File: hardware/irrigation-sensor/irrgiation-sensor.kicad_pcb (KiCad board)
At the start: 2 copper layers, 176 x 40 mm, 35 parts, among them J1 CONUFL001-SMD-T, J2 SHF-105-01-L-D-TH, Q1 PMV250EPEA, Q2 TSM260P02, U1 24LC32, U2 RFM95W, U3 TLV61225, U4 STM32L412KB

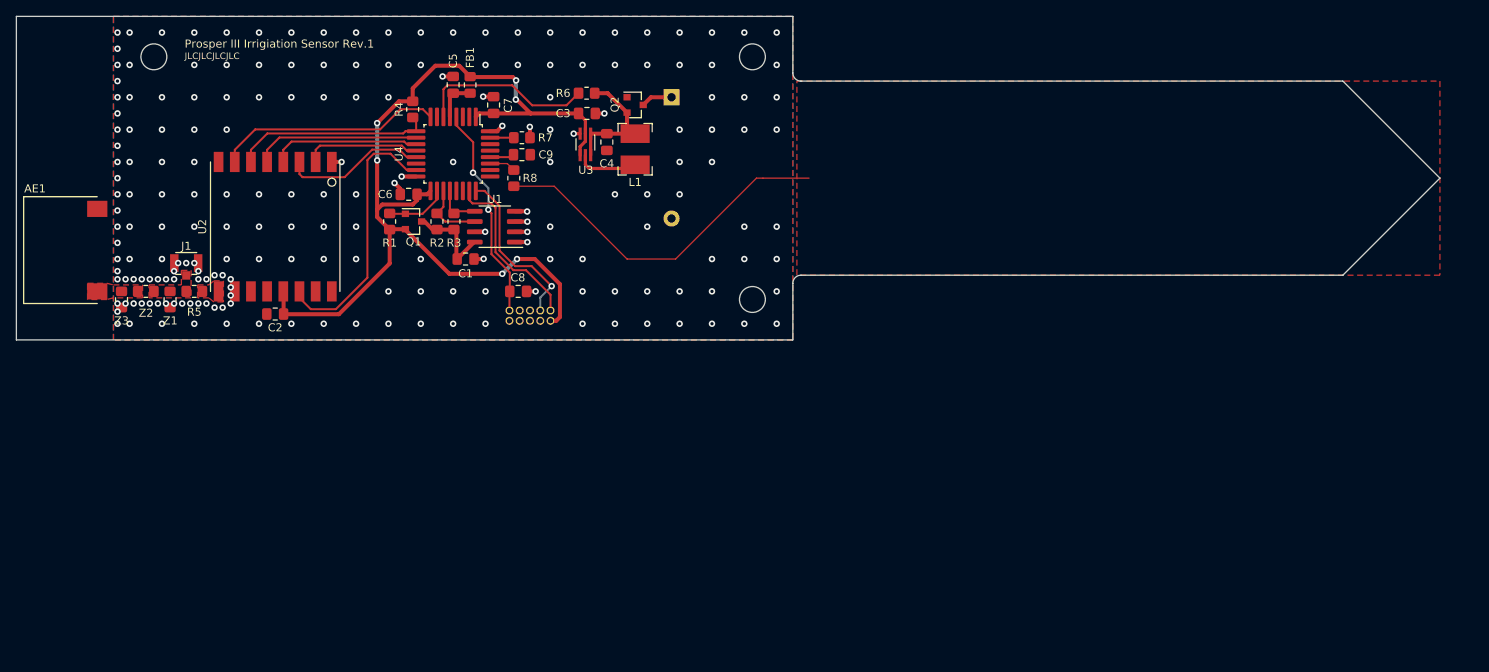
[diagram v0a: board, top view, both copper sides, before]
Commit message: PCB revision 2, add data packet handling to climate-sensor
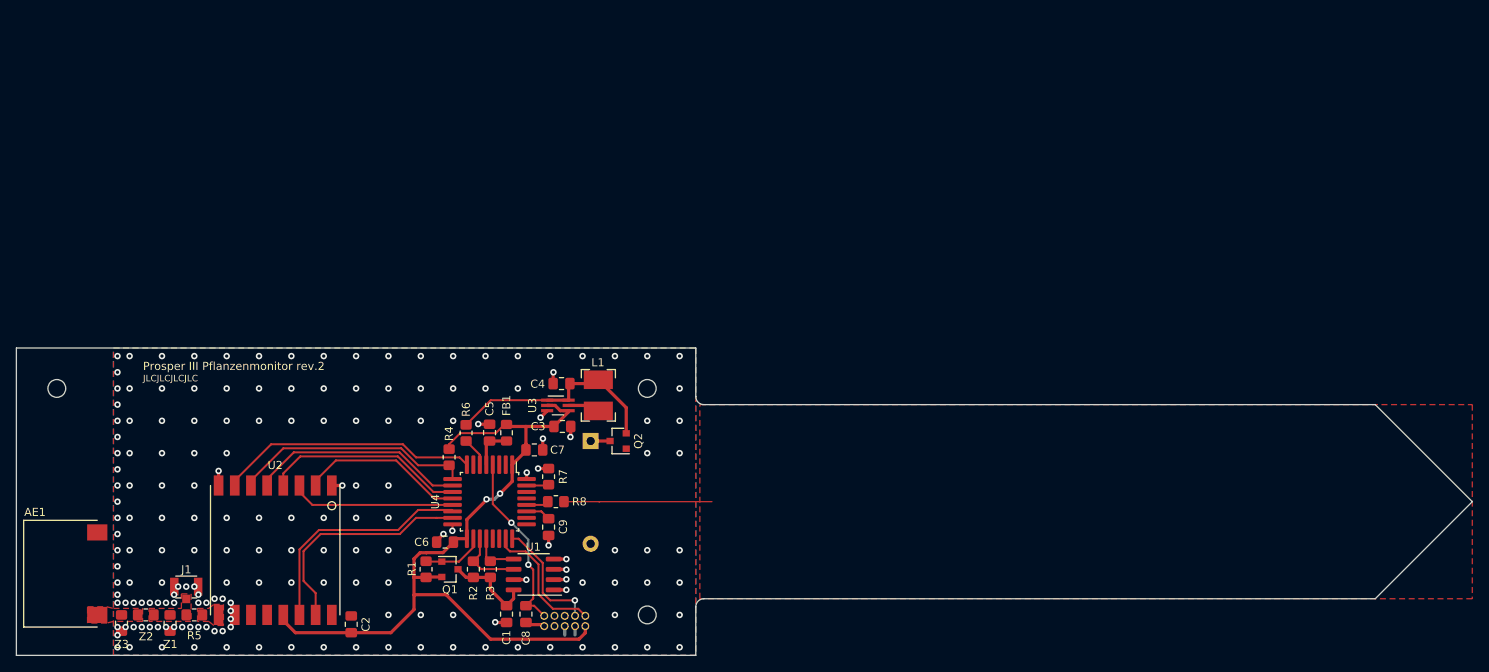
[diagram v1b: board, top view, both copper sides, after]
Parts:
- added G***: LOGO, my-footprints-library:ProsperIIIKlimaMonitorLogo, B.Cu at (65.0, 100.0)
- BT1: footprint my-footprints-library:BatteryHolder_Keystone_2462_2xAA_NoSilkscreen -> my-footprints-library:BatteryHolder_Keystone_2468_2xAAA_NoSilkscreen
- H1, H2, H3: footprint MountingHole:MountingHole_3.2mm_M3 -> MountingHole:MountingHole_2.2mm_M2
- moved C9 46.2 mm to (125.8, 103.1), turned to 270 degrees
- moved R6 44.6 mm to (115.6, 91.5), turned to 270 degrees
- moved C1 44.2 mm to (120.6, 113.9), turned to 270 degrees
- moved BT1 43.7 mm to (131.0, 92.5)
- moved U1 43.3 mm to (124.0, 109.0)
- moved C5 43.2 mm to (118.5, 91.5)
- moved C6 43.2 mm to (113.0, 105.0)
- moved Q1 43.2 mm to (113.6, 108.4)
- moved R1 43.2 mm to (110.7, 108.4)
- moved R2 43.2 mm to (116.5, 108.4)
- moved R3 43.2 mm to (118.6, 108.4)
- moved R4 43.2 mm to (113.5, 94.5)
- moved U4 43.2 mm to (118.5, 100.0)
- moved FB1 43.2 mm to (120.6, 91.5)
- moved H2 43.0 mm to (138.0, 86.0)
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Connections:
- C9 pad 1: TSC_IO2 -> TSC_IO1
- R8 pad 1: TSC_IO1 -> TSC_IO2
- U2 pad 14: RFM95_IRQ -> RFM95_DIO0
- U2 pad 15: Net-(U2-Pad15) -> RFM95_DIO1
- U4 pad 14: Net-(U4-Pad14) -> RFM95_DIO0
- U4 pad 15: RFM95_IRQ -> RFM95_DIO1
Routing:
- net RFM95_IRQ: track 33.1 -> 0.00 mm
- net RFM95_DIO0: track 0.00 -> 29.2 mm
- net RFM95_DIO1: track 0.00 -> 28.6 mm
- net SENSOR_PLANE: track 44.4 -> 18.4 mm
- net +3V3: track 120.7 -> 98.8 mm, vias 6 -> 2
- net Net-(R6-Pad2): track 22.0 -> 3.63 mm
- net VIN_SENSE: track 16.1 -> 27.8 mm
- net GND: track 22.2 -> 29.5 mm, vias 202 -> 183
- net SCK: track 18.5 -> 25.1 mm
- net RFM95_NSS: track 20.6 -> 26.8 mm
- net MISO: track 14.4 -> 20.5 mm
- net SWCLK: track 21.1 -> 15.0 mm
- net RFM95_NRST: track 24.8 -> 29.5 mm
- net SWDIO: track 21.2 -> 16.6 mm
- net NRST: track 26.7 -> 22.7 mm
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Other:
- board size 176 x 40 mm -> 180 x 38 mm
- board text added: "Prosper III Pflanzenmonitor rev.2"
- board text removed: "Prosper III Irrigiation Sensor Rev.1"

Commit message: Implement user management and authorization
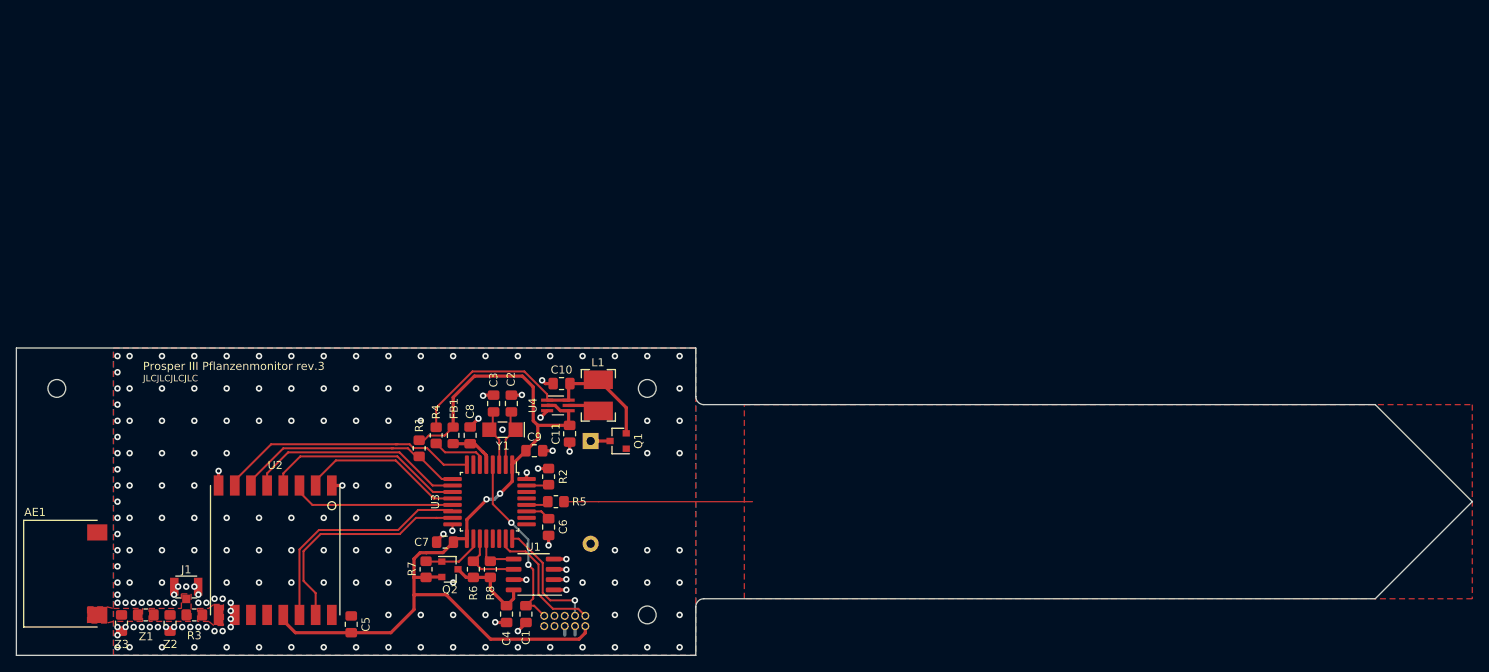
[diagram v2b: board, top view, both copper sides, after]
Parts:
- removed the G*** at (65.0, 100.0)
- added C2: 100nF, Capacitor_SMD:C_0805_2012Metric_Pad1.18x1.45mm_HandSolder, F.Cu at (121.2, 87.9)
- added C3: 100nF, Capacitor_SMD:C_0805_2012Metric_Pad1.18x1.45mm_HandSolder, F.Cu at (119.0, 87.9)
- added G***: LOGO, my-footprints-library:ProsperIIIPflanzenMonitorLogo, B.Cu at (66.0, 103.5)
- added Y1: 32768Hz, Crystal:Crystal_SMD_EuroQuartz_EQ161-2Pin_3.2x1.5mm_HandSoldering, F.Cu at (120.1, 91.1)
- moved FB1 6.61 mm to (114.0, 91.8)
- moved R1 3.86 mm to (109.8, 93.4)
- moved R4 3.71 mm to (111.9, 91.8)
- moved C8 2.42 mm to (116.1, 91.8)
- moved C11 1.27 mm to (128.4, 91.6), turned to 270 degrees
- moved C9 0.10 mm to (124.0, 93.7)
- renumbered C8 to C1, C4 to C10, C3 to C11, C1 to C4, C2 to C5, C9 to C6, C6 to C7, C5 to C8, C7 to C9, Q2 to Q1, Q1 to Q2, R4 to R1, R7 to R2, R5 to R3, R6 to R4, R8 to R5, R2 to R6, R1 to R7, R3 to R8, U4 to U3, U3 to U4, Z2 to Z1, Z1 to Z2
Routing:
- net +3V3: track 98.8 -> 112.9 mm
- net VIN_SENSE: track 27.8 -> 36.4 mm
- net Net-(C2-Pad1): track 0.00 -> 7.27 mm
- net Net-(C3-Pad1): track 0.00 -> 7.23 mm
- net SENSOR_PLANE: track 18.4 -> 23.3 mm
- net Net-(R4-Pad2): track 3.63 -> 7.11 mm
- net GND: track 29.5 -> 31.6 mm, vias 183 -> 185
- net +3.3VA: track 5.19 -> 5.86 mm
- net RFM95_NRST: track 29.5 -> 29.0 mm
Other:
- board text added: "Prosper III Pflanzenmonitor rev.3"
- board text removed: "Prosper III Pflanzenmonitor rev.2"

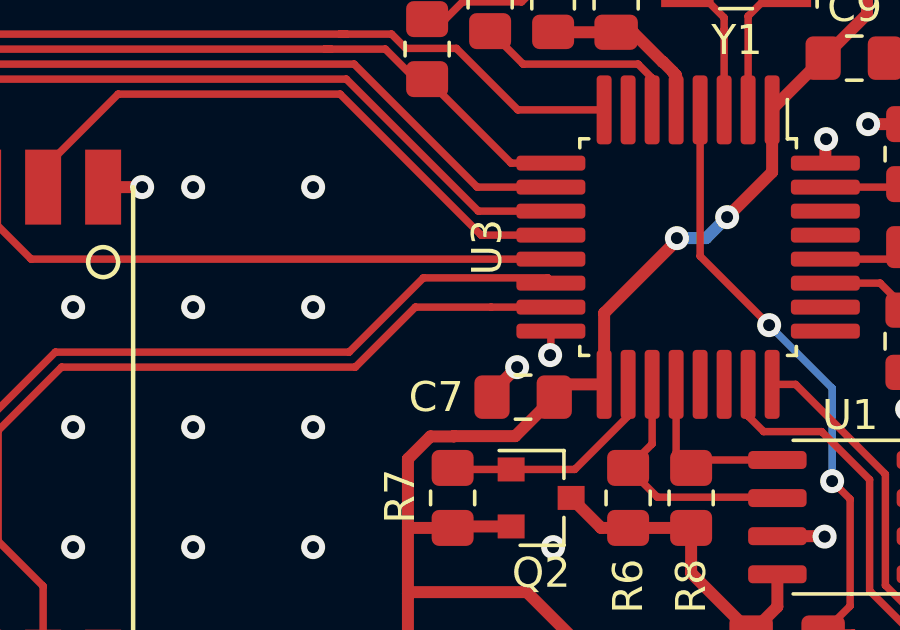
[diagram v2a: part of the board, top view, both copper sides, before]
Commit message: Implement downlink functionality
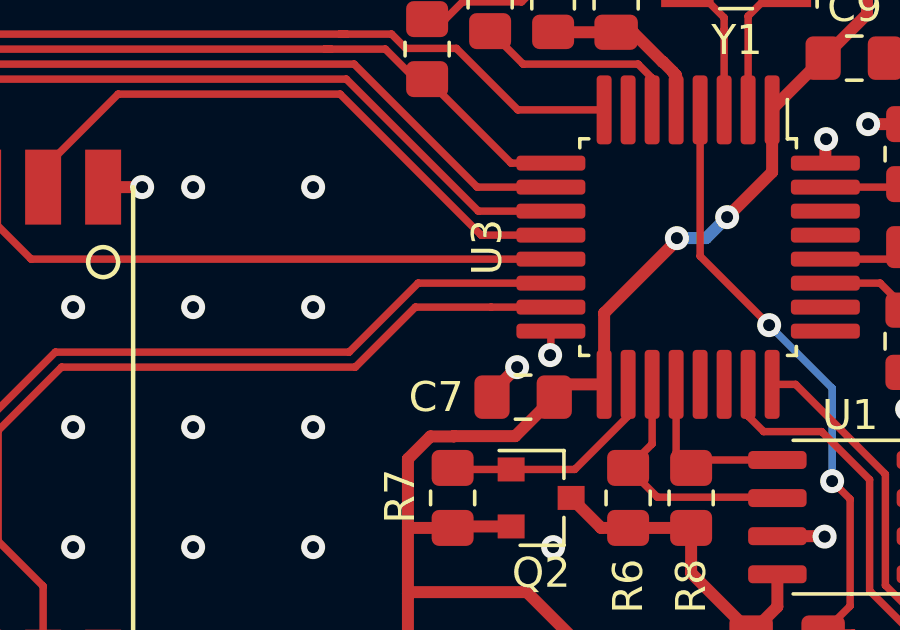
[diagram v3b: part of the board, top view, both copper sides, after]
